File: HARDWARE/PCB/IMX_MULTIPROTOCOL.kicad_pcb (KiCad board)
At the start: 2 copper layers, 68.6 x 53.3 mm, 16 parts, among them J17 Conn_01x08, J18 Conn_01x06, J19 Conn_01x10, J20 Conn_01x08

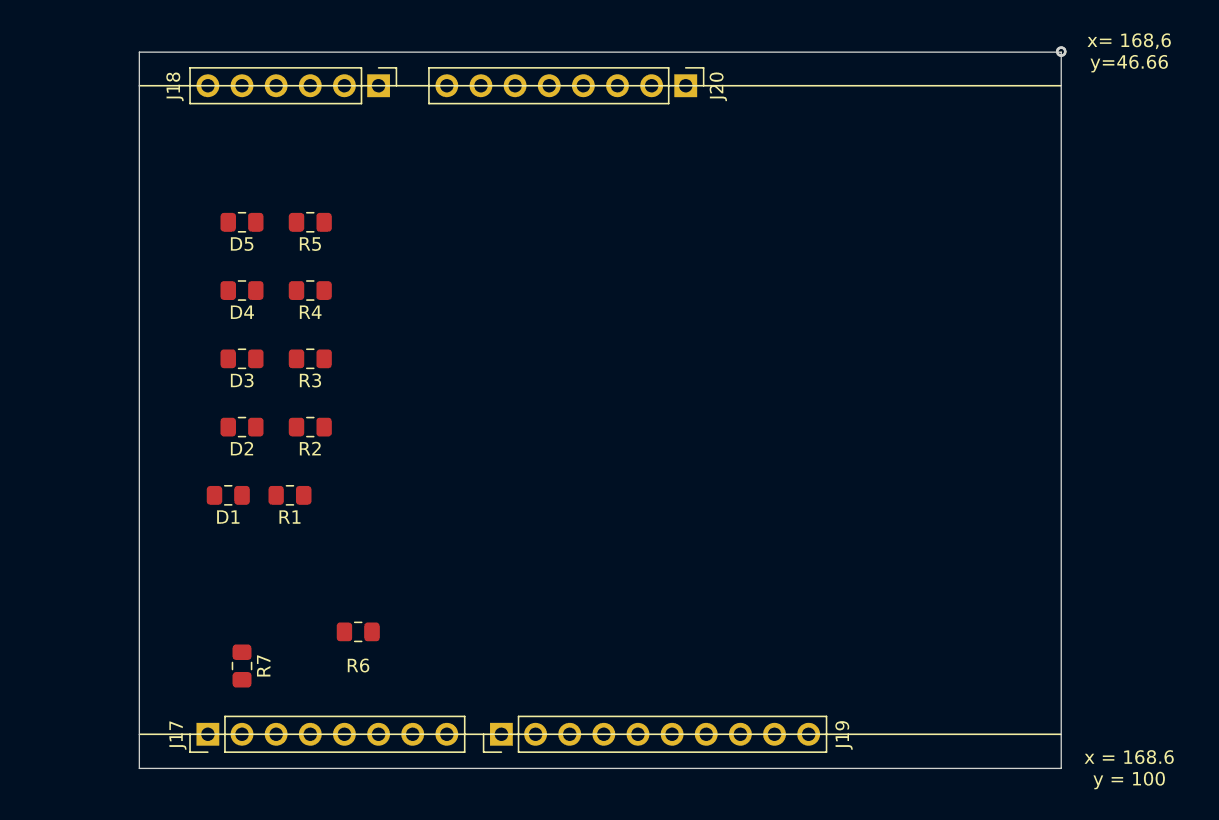
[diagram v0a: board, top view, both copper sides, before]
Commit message: FIRMWARE: USB fix, Led rework,
HARDWARE: Led rework
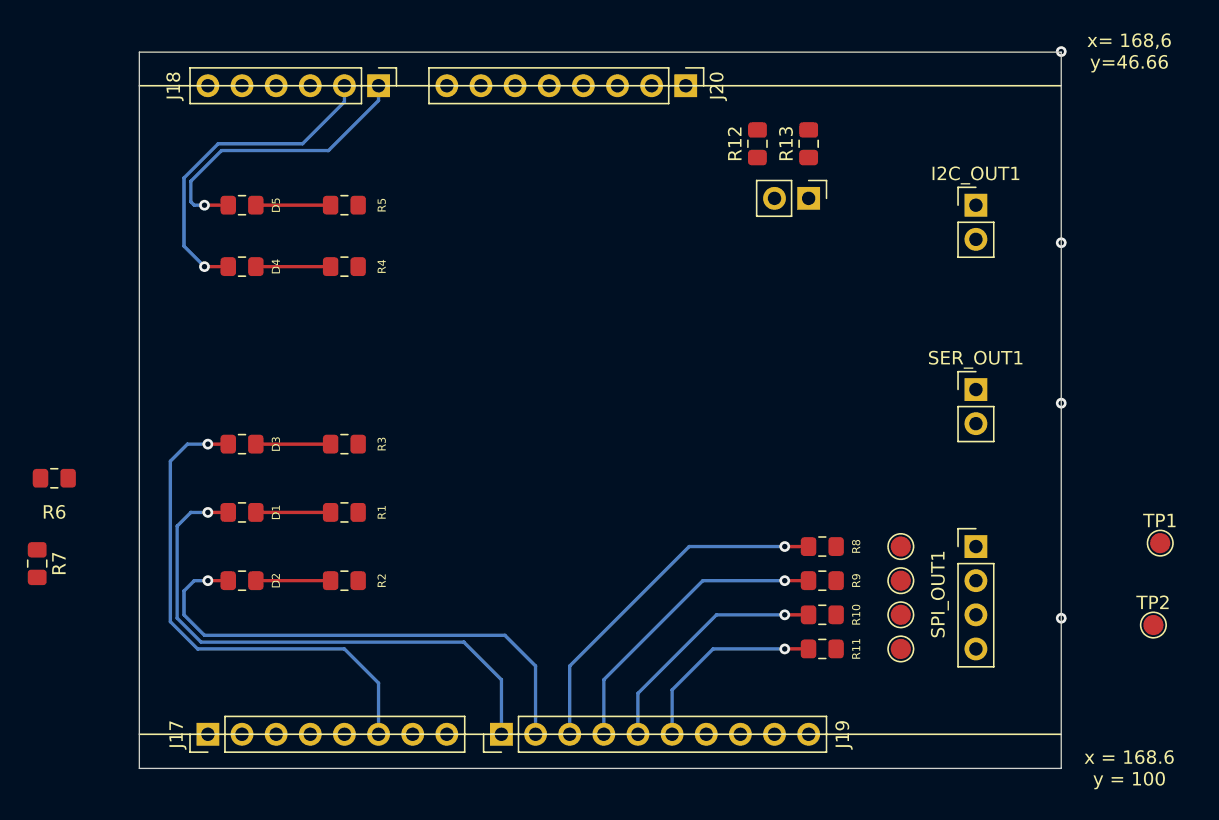
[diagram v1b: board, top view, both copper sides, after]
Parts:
- added I2C_OUT1: Conn_01x02, Connector_PinHeader_2.54mm:PinHeader_1x02_P2.54mm_Vertical, F.Cu at (162.2, 58.1)
- added I2C_PULLUP_ENABLE1: Conn_01x02, Connector_PinHeader_2.54mm:PinHeader_1x02_P2.54mm_Vertical, F.Cu at (149.8, 57.6)
- added R10: 100R, Resistor_SMD:R_0805_2012Metric_Pad1.15x1.40mm_HandSolder, F.Cu at (150.8, 88.6)
- added R11: 100R, Resistor_SMD:R_0805_2012Metric_Pad1.15x1.40mm_HandSolder, F.Cu at (150.8, 91.1)
- added R12: 10k, Resistor_SMD:R_0805_2012Metric_Pad1.15x1.40mm_HandSolder, F.Cu at (146.0, 53.5)
- added R13: 10k, Resistor_SMD:R_0805_2012Metric_Pad1.15x1.40mm_HandSolder, F.Cu at (149.8, 53.5)
- added R8: 100R, Resistor_SMD:R_0805_2012Metric_Pad1.15x1.40mm_HandSolder, F.Cu at (150.8, 83.5)
- added R9: 100R, Resistor_SMD:R_0805_2012Metric_Pad1.15x1.40mm_HandSolder, F.Cu at (150.8, 86.0)
- added SER_OUT1: Conn_01x02, Connector_PinHeader_2.54mm:PinHeader_1x02_P2.54mm_Vertical, F.Cu at (162.2, 71.8)
- added SPI_OUT1: Conn_01x04, Connector_PinHeader_2.54mm:PinHeader_1x04_P2.54mm_Vertical, F.Cu at (162.2, 83.5)
- added TP1: TestPoint, TestPoint:TestPoint_Pad_D1.5mm, F.Cu at (176.0, 83.2)
- added TP2: TestPoint, TestPoint:TestPoint_Pad_D1.5mm, F.Cu at (175.5, 89.3)
- added TP3: TestPoint, TestPoint:TestPoint_Pad_D1.5mm, F.Cu at (156.7, 83.5)
- added TP4: TestPoint, TestPoint:TestPoint_Pad_D1.5mm, F.Cu at (156.7, 86.0)
- added TP5: TestPoint, TestPoint:TestPoint_Pad_D1.5mm, F.Cu at (156.7, 88.6)
- added TP6: TestPoint, TestPoint:TestPoint_Pad_D1.5mm, F.Cu at (156.7, 91.1)
- moved R6 25.3 mm to (93.7, 78.4)
- moved R7 17.0 mm to (92.4, 84.8)
- moved R2 11.7 mm to (115.3, 86.0)
- moved D2 11.4 mm to (107.6, 86.0)
- moved R3 6.84 mm to (115.3, 75.9)
- moved D3 6.35 mm to (107.6, 75.9)
- moved R1 4.25 mm to (115.3, 81.0)
- moved R4 3.10 mm to (115.3, 62.7)
- moved R5 2.84 mm to (115.3, 58.1)
- moved D4 1.78 mm to (107.6, 62.7)
- moved D1 1.63 mm to (107.6, 81.0)
- moved D5 1.27 mm to (107.6, 58.1)
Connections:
- J17 pad 3: SPI_LED_GPIO_AD_B0_09 -> Net-(J17-Pad3)
- J17 pad 4: I2C_LED_GPIO_AD_B0_07 -> Net-(J17-Pad4)
- J17 pad 7: TX_LED_GPIO_AD_B0_14 -> Net-(J17-Pad7)
- J17 pad 8: RX_LED_GPIO_AD_B1_06 -> Net-(J17-Pad8)
- J18 pad 1: Net-(J18-Pad1) -> RX_LED_GPIO_AD_B1_06
- J18 pad 2: Net-(J18-Pad2) -> TX_LED_GPIO_AD_B0_14
- J19 pad 1: Net-(J19-Pad1) -> SPI_LED_GPIO_AD_B0_09
- J19 pad 2: Net-(J19-Pad2) -> I2C_LED_GPIO_AD_B0_07
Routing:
- net SPI_LED_GPIO_AD_B0_09: track 0.00 -> 41.2 mm, vias 0 -> 1
- net I2C_LED_GPIO_AD_B0_07: track 0.00 -> 38.2 mm, vias 0 -> 1
- net SERIAL_LED_GPIO_AD_B0_06: track 0.00 -> 38.0 mm, vias 0 -> 1
- net LPSPI_CS_GPIO_AD_B0_11: track 0.00 -> 26.5 mm, vias 0 -> 1
- net TX_LED_GPIO_AD_B0_14: track 0.00 -> 24.5 mm, vias 0 -> 1
- net LPSPI_MOSI_GPIO_AD_B0_12: track 0.00 -> 22.3 mm, vias 0 -> 1
- net RX_LED_GPIO_AD_B1_06: track 0.00 -> 22.0 mm, vias 0 -> 1
- net LPSPI_MISO_GPIO_AD_B0_13: track 0.00 -> 18.2 mm, vias 0 -> 1
- net LPSPI_CLK_GPIO_AD_B0_10: track 0.00 -> 14.7 mm, vias 0 -> 1
- net Net-(D5-Pad1): track 0.00 -> 5.57 mm
- net Net-(D4-Pad1): track 0.00 -> 5.57 mm
- net Net-(D3-Pad1): track 0.00 -> 5.57 mm
- net Net-(D2-Pad1): track 0.00 -> 5.57 mm
- net Net-(D1-Pad1): track 0.00 -> 5.57 mm
- net (no net): vias 1 -> 4
